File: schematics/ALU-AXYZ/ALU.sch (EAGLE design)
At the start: 210 parts, among them T0 1k, T1 1k, T2 1k, T3 1k, T4 1k, T5 1k, T6 1k, T7 1k, X0 220, X1 220, X2 220, X3 220, X4 220, X5 220, X6 220, X7 220, Y0 220, Y1 220, Y2 220, Y3 220, Y4 220, Y5 220, Y6 220, Y7 220

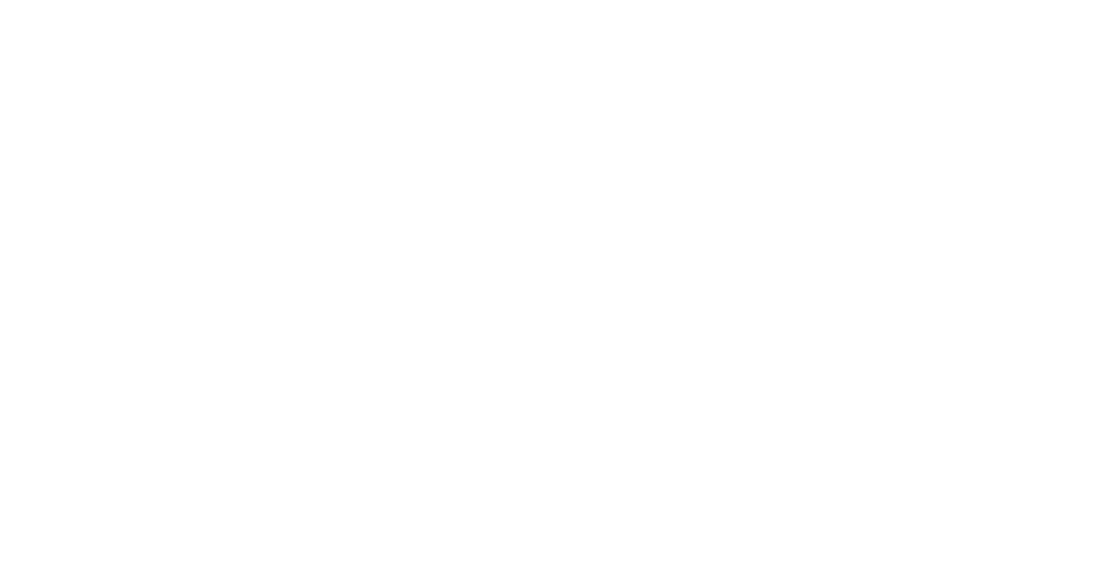
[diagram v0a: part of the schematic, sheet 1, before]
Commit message: Added few caps to power line.
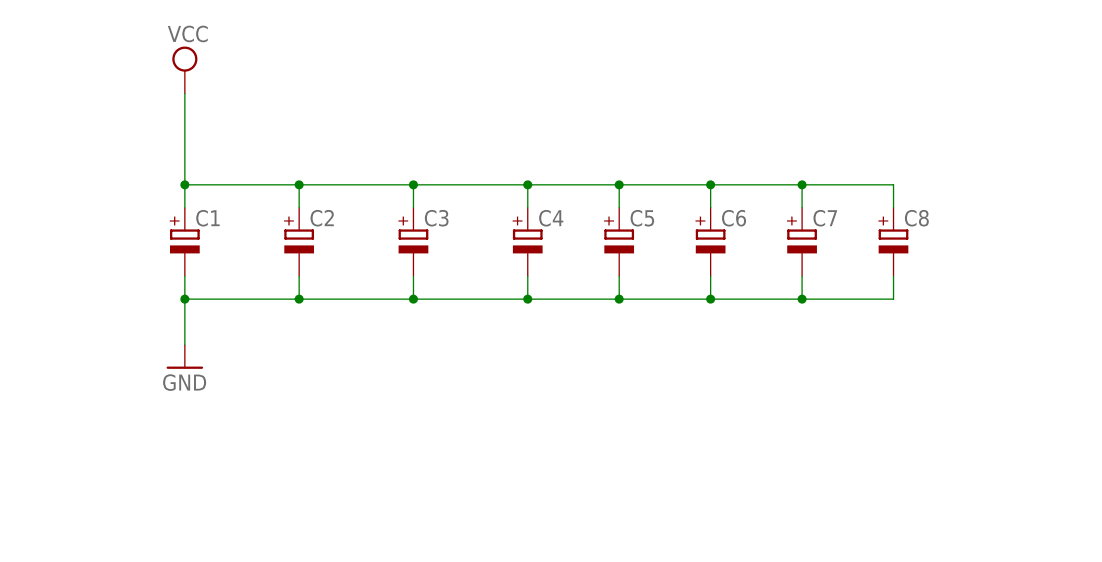
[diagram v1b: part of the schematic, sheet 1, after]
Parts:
- added C1, C2, C3, C4, C5, C6, C7, C8: (no value), rcl:CPOL-EUE3.5-8
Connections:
- net GND: now also C1.-, C2.-, C3.-, C4.-, C5.-, C6.-, C7.-, C8.-
- net VCC: now also C1.+, C2.+, C3.+, C4.+, C5.+, C6.+, C7.+, C8.+
